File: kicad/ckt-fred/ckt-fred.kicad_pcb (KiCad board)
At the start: 2 copper layers, 73.7 x 38.1 mm, 41 parts, among them J1 Screw_Terminal_01x02, J2 AVR-ISP, J3 8P8C, J4 8P8C, J5 Screw_Terminal_01x02, SW1 FSM4JSMATR, T1 PE-51687, U1 AP7381-33Y, U2 INA180A4, U3 ATtiny85-20S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

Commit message: Start of FRED PCB
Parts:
- removed C3: 1uF, Capacitor_SMD:C_0805_2012Metric
- removed C4, C6: 0.1uF, Capacitor_SMD:C_0805_2012Metric
- removed D6: GREEN LED, LED_SMD:LED_0805_2012Metric
- removed D7: RED LED, LED_SMD:LED_0805_2012Metric
- removed D8: AMBER LED, LED_SMD:LED_0805_2012Metric
- removed D9: SMAJ18A-TP, Diode_SMD:D_SMA
- removed F1: 1210L020WR, Resistor_SMD:R_1210_3225Metric
- removed H1, H2, H3, H4: MountingHole, MountingHole:MountingHole_3.2mm_M3_Pad
- removed J1, J5: Screw_Terminal_01x02, TerminalBlock_RND:TerminalBlock_RND_205-00012_1x02_P5.00mm_Horizontal
- removed J3, J4: 8P8C, Connector_RJ:RJ45_Amphenol_54602-x08_Horizontal
- removed R3: 1k, Resistor_SMD:R_0805_2012Metric
- removed R4: 510, Resistor_SMD:R_0805_2012Metric
- removed R5: 100k, Resistor_SMD:R_0805_2012Metric
- removed R6: 330, Resistor_SMD:R_0805_2012Metric
- removed SW1: FSM4JSMATR, ISE_Generic:TE_FSM4JSMA
- removed T1: PE-51687, ISE_Generic:XFMR_PE-51687
- removed U4: TLP241A, ISE_UltraLibrarian:11-5B201S_TOS
- added BT1: Battery_Cell, Battery:BatteryHolder_Keystone_3034_1x20mm, F.Cu at (37.1, 179.1)
- added JP1: SolderJumper_2_Open, Jumper:SolderJumper-2_P1.3mm_Open_RoundedPad1.0x1.5mm, F.Cu at (66.2, 168.1)
- D5: value BAV99 -> BAT43W; footprint Package_TO_SOT_SMD:SOT-23 -> ISE_Generic:SOD-123T
- R1: value 1k -> 100k
- R2: value 1k -> 330
- TP1, TP2, TP3, TP4: moved to F.Cu
- U2: value INA180A4 -> DRV5032; footprint Package_TO_SOT_SMD:SOT-23-5 -> Package_TO_SOT_SMD:SOT-23
- U3: value ATtiny85-20S -> ATtiny13-20SS; footprint ISE_Generic:ATMEL_SO8_DUAL -> Package_SO:SOIC-8_3.9x4.9mm_P1.27mm
- moved TP2 31.9 mm to (58.5, 170.4), turned to 0 degrees
- moved D4 27.6 mm to (52.8, 185.3), turned to 0 degrees
- moved U2 24.6 mm to (73.3, 187.3), turned to 0 degrees
- moved TP1 24.5 mm to (52.2, 170.4), turned to 0 degrees
- moved D5 23.0 mm to (49.8, 189.5), turned to 180 degrees
- moved D1 20.0 mm to (52.8, 175.0), turned to 180 degrees
- moved D2 18.5 mm to (52.8, 178.4), turned to 180 degrees
- moved C1 18.4 mm to (59.7, 178.1), turned to -90 degrees
- moved D3 18.2 mm to (52.8, 181.9), turned to 0 degrees
- moved J2 17.9 mm to (66.2, 173.6)
- moved U1 16.9 mm to (59.7, 186.4), turned to 90 degrees
- moved R1 13.5 mm to (64.4, 189.9), turned to 0 degrees
- moved C5 12.0 mm to (65.9, 178.7)
- moved U3 12.0 mm to (66.8, 184.2), turned to 90 degrees
- moved C2 7.81 mm to (55.0, 188.6), turned to 180 degrees
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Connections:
- D5 pad 1: Net-(C6-Pad1) -> +3.3V
- D5 pad 2: Net-(C6-Pad1) -> Net-(BT1-Pad1)
- R1 pad 1: Net-(D6-Pad2) -> +3.3V
- R1 pad 2: +3.3V -> Net-(U2-Pad2)
- R2 pad 1: Net-(J2-Pad1) -> Net-(J2-Pad3)
- R2 pad 2: Net-(D7-Pad2) -> Net-(R2-Pad2)
- TP3 pad 1: /MSS_OCC -> GND
- TP4 pad 1: /MSS_GND -> Net-(R2-Pad2)
- U2 pad 1: Net-(R5-Pad2) -> +3.3V
- U2 pad 2: GND -> Net-(U2-Pad2)
- U2 pad 3: Net-(C6-Pad1) -> GND
- U3 pad 2: /~{CAL_SW} -> Net-(U3-Pad2)
- U3 pad 3: /DCC_CURRENT -> Net-(U2-Pad2)
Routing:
- net GND: track 74.5 -> 23.9 mm, vias 25 -> 30
- net /MSS_OCC: track 40.6 -> 0.00 mm, vias 3 -> 0
- net Net-(U3-Pad2): track 0.00 -> 36.7 mm
- net Net-(J3-Pad3): track 32.4 -> 0.00 mm
- net Net-(J3-Pad8): track 28.1 -> 0.00 mm, vias 1 -> 0
- net Net-(J3-Pad7): track 27.4 -> 0.00 mm, vias 1 -> 0
- net Net-(C6-Pad1): track 26.1 -> 0.00 mm
- net Net-(J3-Pad1): track 21.3 -> 0.00 mm
- net /~{CAL_SW}: track 20.7 -> 0.00 mm
- net Net-(J2-Pad1): track 27.4 -> 7.97 mm
- net Net-(D2-Pad2): track 34.7 -> 18.6 mm
- net Net-(J2-Pad4): track 28.5 -> 13.1 mm, vias 4 -> 2
- net /MSS_GND: track 13.2 -> 0.00 mm, vias 3 -> 0
- net Net-(U2-Pad2): track 0.00 -> 11.0 mm
- net +3.3V: track 61.8 -> 50.8 mm
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- added copper zone on F.Cu, net Net-(BT1-Pad1)
- added copper zone on F.Cu, net Net-(D1-Pad2)
- added copper zone on F.Cu, net Net-(D2-Pad2)
- added copper zone on F.Cu, net Net-(R2-Pad2)
- removed copper zone on B.Cu, net /MSS_GND
- removed copper zone on F.Cu, net /~{CAL_SW}
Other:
- board size 73.7 x 38.1 mm -> 50.8 x 25.4 mm
- board text added: "+ LED -"
- board text added: "CR2032 Coin Cell"
- board text added: "Iowa Scaled Engineering CKT-FRED v1.0 CC BY-SA ©2024 www.iascaled.com"
- board text added: "Track Power"
- board text removed: "6-24 Volts DC/AC/DCC"
- board text removed: "AUX DETECT"
- board text removed: "CAL"
- board text removed: "DETECT"
- board text removed: "GND"
- board text removed: "IN"
- board text removed: "Iowa Scaled Engineering MSS-CROSSOVER v2.1 www.iascaled.com ©2024"
- board text removed: "MSS"
- board text removed: "POWER"
- board text removed: "PWR"

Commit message: A few updates
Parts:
- TP1, TP2, TP3, TP4: footprint TestPoint:TestPoint_Pad_D2.0mm -> TestPoint:TestPoint_Pad_4.0x4.0mm
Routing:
- net GND: vias 30 -> 27
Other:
- board text added: "Magnet Sw"

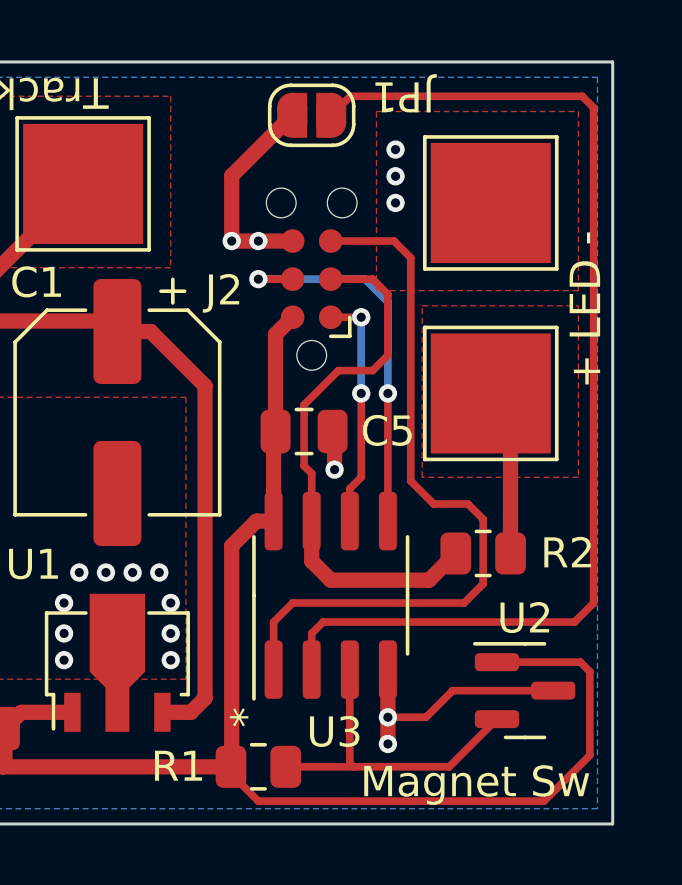
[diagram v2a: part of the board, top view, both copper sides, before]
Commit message: Add output jumper to bypass resistor
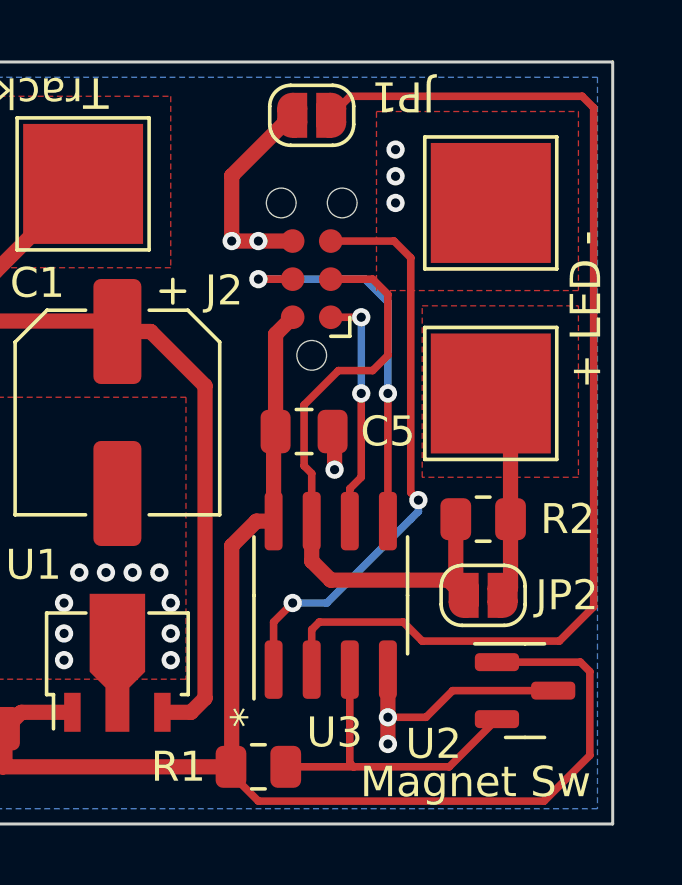
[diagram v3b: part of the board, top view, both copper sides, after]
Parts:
- added JP2: SolderJumper_2_Open, Jumper:SolderJumper-2_P1.3mm_Open_RoundedPad1.0x1.5mm, F.Cu at (71.9, 184.2)
- moved R2 1.14 mm to (71.9, 181.6)
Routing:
- net Net-(J2-Pad5): track 24.5 -> 19.4 mm, vias 0 -> 2
- net Net-(J2-Pad3): track 18.4 -> 21.1 mm
- net Net-(R2-Pad2): track 5.61 -> 7.11 mm
- net Net-(JP1-Pad2): track 36.7 -> 37.4 mm
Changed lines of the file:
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@@
       (net 9 "Net-(R2-Pad2)") (pinfunction "1") (pintype "passive"))
+  )
+  (footprint "Jumper:SolderJumper-2_P1.3mm_Open_RoundedPad1.0x1.5mm" (layer "F.Cu")
+    (at 71.882 184.15)
+    (descr "SMD Solder Jumper, 1x1.5mm, rounded Pads, 0.3mm gap, open")
+    (tags "solder jumper open")
+    (property "Sheetfile" "ckt-fred.kicad_sch")
+    (property "Sheetname" "")
+    (attr exclude_from_pos_files)
+    (fp_text reference "JP2" (at 2.794 0) (layer "F.SilkS")
+      (effects (font (size 1 1) (thickness 0.15)))
+    )
+    (fp_text value "SolderJumper_2_Open" (at 0 1.9) (layer "F.Fab")
+      (effects (font (size 1 1) (thickness 0.15)))
+    )
+    (fp_line (start -1.4 0.3) (end -1.4 -0.3) (layer "F.SilkS") (width 0.12))
+    (fp_line (start 1.4 -0.3) (end 1.4 0.3) (layer "F.SilkS") (width 0.12))
+    (fp_line (start -0.7 -1) (end 0.7 -1) (layer "F.SilkS") (width 0.12))
+    (fp_line (start 0.7 1) (end -0.7 1) (layer "F.SilkS") (width 0.12))
+    (fp_arc (start -0.7 1) (mid -1.194975 0.794975) (end -1.4 0.3) (layer "F.SilkS") (width 0.12))
+    (fp_arc (start 1.4 0.3) (mid 1.194975 0.794975) (end 0.7 1) (layer "F.SilkS") (width 0.12))
+    (fp_arc (start -1.4 -0.3) (mid -1.194975 -0.794975) (end -0.7 -1) (layer "F.SilkS") (width 0.12))
+    (fp_arc (start 0.7 -1) (mid 1.194975 -0.794975) (end 1.4 -0.3) (layer "F.SilkS") (width 0.12))
+    (fp_line (start 1.65 1.25) (end 1.65 -1.25) (layer "F.CrtYd") (width 0.05))
+    (fp_line (start -1.65 -1.25) (end 1.65 -1.25) (layer "F.CrtYd") (width 0.05))
+    (fp_line (start 1.65 1.25) (end -1.65 1.25) (layer "F.CrtYd") (width 0.05))
+    (fp_line (start -1.65 -1.25) (end -1.65 1.25) (layer "F.CrtYd") (width 0.05))
+    (pad "1" smd custom (at -0.65 0) (size 1 0.5) (layers "F.Cu" "F.Mask")
+      (net 10 "Net-(J2-Pad3)") (pinfunction "A") (pintype "passive") (zone_connect 2)
+      (options (clearance outline) (anchor rect))
+      (primitives
+        (gr_circle (center 0 0.25) (end 0.5 0.25) (width 0) (fill yes))
+        (gr_circle (center 0 -0.25) (end 0.5 -0.25) (width 0) (fill yes))
+        (gr_poly (pts
+            (xy 0.5 0.75)
+            (xy 0 0.75)
+            (xy 0 -0.75)
+            (xy 0.5 -0.75)
+          ) (width 0) (fill yes))
+      ))
+    (pad "2" smd custom (at 0.65 0) (size 1 0.5) (layers "F.Cu" "F.Mask")
+      (net 9 "Net-(R2-Pad2)") (pinfunction "B") (pintype "passive") (zone_connect 2)
+      (options (clearance outline) (anchor rect))
+      (primitives
+        (gr_circle (center 0 0.25) (end 0.5 0.25) (width 0) (fill yes))
+        (gr_circle (center 0 -0.25) (end 0.5 -0.25) (width 0) (fill yes))
+        (gr_poly (pts
+            (xy 0 0.75)
+            (xy -0.5 0.75)
+            (xy -0.5 -0.75)
+            (xy 0 -0.75)
+          ) (width 0) (fill yes))
+      ))
   )
   (footprint "Capacitor_SMD:CP_Elec_6.3x5.8" (layer "F.Cu")
@@
   )
   (footprint "Resistor_SMD:R_0805_2012Metric" (layer "F.Cu")
-    (at 71.882 182.753)
+    (at 71.882 181.61)
     (descr "Resistor SMD 0805 (2012 Metric), square (rectangular) end terminal, IPC_7351 nominal, (Body size source: IPC-SM-782 page 72, https://www.pcb-3d.com/wordpress/wp-content/uploads/ipc-sm-782a_amendment_1_and_2.pdf), generated with kicad-footprint-generator")
     (tags "resistor")
@@
     (property "Sheetname" "")
     (attr smd)
-    (fp_text reference "U2" (at 0 -2.4) (layer "F.SilkS")
+    (fp_text reference "U2" (at -3.048 1.778) (layer "F.SilkS")
       (effects (font (size 1 1) (thickness 0.15)))
     )
@@
   (segment (start 52.451 181.864) (end 52.832 181.483) (width 0.508) (layer "F.Cu") (net 5))
   (segment (start 75.184 167.513) (end 67.452 167.513) (width 0.254) (layer "F.Cu") (net 7))
-  (segment (start 66.548 185.039) (end 74.93 185.039) (width 0.254) (layer "F.Cu") (net 7))
+  (segment (start 74.422 185.674) (end 75.565 184.531) (width 0.254) (layer "F.Cu") (net 7))
+  (segment (start 66.167 186.625) (end 66.167 185.293) (width 0.254) (layer "F.Cu") (net 7))
   (segment (start 75.565 167.894) (end 75.184 167.513) (width 0.254) (layer "F.Cu") (net 7))
-  (segment (start 66.167 185.42) (end 66.548 185.039) (width 0.254) (layer "F.Cu") (net 7))
-  (segment (start 74.93 185.039) (end 75.565 184.404) (width 0.254) (layer "F.Cu") (net 7))
+  (segment (start 66.421 185.039) (end 69.215 185.039) (width 0.254) (layer "F.Cu") (net 7))
+  (segment (start 75.565 184.531) (end 75.565 167.894) (width 0.254) (layer "F.Cu") (net 7))
   (segment (start 67.452 167.513) (end 66.817 168.148) (width 0.254) (layer "F.Cu") (net 7))
-  (segment (start 66.167 186.625) (end 66.167 185.42) (width 0.254) (layer "F.Cu") (net 7))
-  (segment (start 75.565 184.404) (end 75.565 167.894) (width 0.254) (layer "F.Cu") (net 7))
+  (segment (start 66.167 185.293) (end 66.421 185.039) (width 0.254) (layer "F.Cu") (net 7))
+  (segment (start 69.215 185.039) (end 69.85 185.674) (width 0.254) (layer "F.Cu") (net 7))
+  (segment (start 69.85 185.674) (end 74.422 185.674) (width 0.254) (layer "F.Cu") (net 7))
   (segment (start 65.3015 189.865) (end 67.564 189.865) (width 0.254) (layer "F.Cu") (net 8))
   (segment (start 67.437 186.625) (end 67.437 189.738) (width 0.254) (layer "F.Cu") (net 8))
@@
   (segment (start 67.564 189.865) (end 70.7515 189.865) (width 0.254) (layer "F.Cu") (net 8))
   (segment (start 70.7515 189.865) (end 72.3415 188.275) (width 0.254) (layer "F.Cu") (net 8))
-  (segment (start 72.7945 182.753) (end 72.7945 178.0775) (width 0.508) (layer "F.Cu") (net 9))
-  (segment (start 72.7945 178.0775) (end 72.136 177.419) (width 0.508) (layer "F.Cu") (net 9))
-  (segment (start 66.802 183.642) (end 70.0805 183.642) (width 0.508) (layer "F.Cu") (net 10))
-  (segment (start 66.167 183.007) (end 66.802 183.642) (width 0.508) (layer "F.Cu") (net 10))
-  (segment (start 70.0805 183.642) (end 70.9695 182.753) (width 0.508) (layer "F.Cu") (net 10))
+  (segment (start 72.7945 183.8875) (end 72.532 184.15) (width 0.508) (layer "F.Cu") (net 9))
+  (segment (start 72.136 177.419) (end 72.7945 178.0775) (width 0.508) (layer "F.Cu") (net 9))
+  (segment (start 72.7945 178.0775) (end 72.7945 183.8875) (width 0.508) (layer "F.Cu") (net 9))
+  (segment (start 70.9695 181.61) (end 70.9695 183.8875) (width 0.508) (layer "F.Cu") (net 10))
   (segment (start 65.913 177.8) (end 65.913 179.832) (width 0.254) (layer "F.Cu") (net 10))
+  (segment (start 66.167 181.675) (end 66.167 183.007) (width 0.508) (layer "F.Cu") (net 10))
   (segment (start 68.707 176.149) (end 68.199 176.657) (width 0.254) (layer "F.Cu") (net 10))
   (segment (start 68.199 173.609) (end 68.707 174.117) (width 0.254) (layer "F.Cu") (net 10))
+  (segment (start 70.9695 183.8875) (end 71.232 184.15) (width 0.508) (layer "F.Cu") (net 10))
+  (segment (start 66.802 183.642) (end 70.724 183.642) (width 0.508) (layer "F.Cu") (net 10))
   (segment (start 68.199 176.657) (end 67.056 176.657) (width 0.254) (layer "F.Cu") (net 10))
   (segment (start 66.167 180.086) (end 66.167 181.675) (width 0.254) (layer "F.Cu") (net 10))
-  (segment (start 66.167 181.675) (end 66.167 183.007) (width 0.508) (layer "F.Cu") (net 10))
+  (segment (start 70.724 183.642) (end 71.232 184.15) (width 0.508) (layer "F.Cu") (net 10))
   (segment (start 65.913 179.832) (end 66.167 180.086) (width 0.254) (layer "F.Cu") (net 10))
+  (segment (start 66.167 183.007) (end 66.802 183.642) (width 0.508) (layer "F.Cu") (net 10))
   (segment (start 66.802 173.609) (end 68.199 173.609) (width 0.254) (layer "F.Cu") (net 10))
   (segment (start 67.056 176.657) (end 65.913 177.8) (width 0.254) (layer "F.Cu") (net 10))
   (segment (start 68.707 174.117) (end 68.707 176.149) (width 0.254) (layer "F.Cu") (net 10))
-  (segment (start 70.231 181.102) (end 69.469 180.34) (width 0.254) (layer "F.Cu") (net 11))
-  (segment (start 71.374 181.102) (end 70.231 181.102) (width 0.254) (layer "F.Cu") (net 11))
-  (segment (start 65.532 184.404) (end 71.247 184.404) (width 0.254) (layer "F.Cu") (net 11))
+  (segment (start 69.469 180.721) (end 69.469 172.897394) (width 0.254) (layer "F.Cu") (net 11))
   (segment (start 64.897 186.625) (end 64.897 185.039) (width 0.254) (layer "F.Cu") (net 11))
+  (segment (start 69.469 172.897394) (end 68.910606 172.339) (width 0.254) (layer "F.Cu") (net 11))
+  (segment (start 64.897 185.039) (end 65.532 184.404) (width 0.254) (layer "F.Cu") (net 11))
+  (segment (start 69.723 180.975) (end 69.469 180.721) (width 0.254) (layer "F.Cu") (net 11))
   (segment (start 68.910606 172.339) (end 66.802 172.339) (width 0.254) (layer "F.Cu") (net 11))
-  (segment (start 71.882 181.61) (end 71.374 181.102) (width 0.254) (layer "F.Cu") (net 11))
-  (segment (start 71.247 184.404) (end 71.882 183.769) (width 0.254) (layer "F.Cu") (net 11))
-  (segment (start 64.897 185.039) (end 65.532 184.404) (width 0.254) (layer "F.Cu") (net 11))
-  (segment (start 69.469 180.34) (end 69.469 172.897394) (width 0.254) (layer "F.Cu") (net 11))
-  (segment (start 69.469 172.897394) (end 68.910606 172.339) (width 0.254) (layer "F.Cu") (net 11))
-  (segment (start 71.882 183.769) (end 71.882 181.61) (width 0.254) (layer "F.Cu") (net 11))
+  (via (at 69.723 180.975) (size 0.6096) (drill 0.3048) (layers "F.Cu" "B.Cu") (net 11))
+  (via (at 65.532 184.404) (size 0.6096) (drill 0.3048) (layers "F.Cu" "B.Cu") (net 11))
+  (segment (start 69.723 181.356) (end 69.723 180.975) (width 0.254) (layer "B.Cu") (net 11))
+  (segment (start 66.675 184.404) (end 69.469 181.61) (width 0.254) (layer "B.Cu") (net 11))
+  (segment (start 69.469 181.61) (end 69.723 181.356) (width 0.254) (layer "B.Cu") (net 11))
+  (segment (start 65.532 184.404) (end 66.675 184.404) (width 0.254) (layer "B.Cu") (net 11))
   (segment (start 67.818 174.879) (end 66.802 174.879) (width 0.254) (layer "F.Cu") (net 12))
   (segment (start 67.818 180.213) (end 67.437 180.594) (width 0.254) (layer "F.Cu") (net 12))
